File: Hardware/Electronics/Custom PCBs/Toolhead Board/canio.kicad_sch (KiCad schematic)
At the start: 12 parts, among them J7 Conn_01x02, J8 Conn_01x02, J9 120TR, U5 SN65HVD1050D

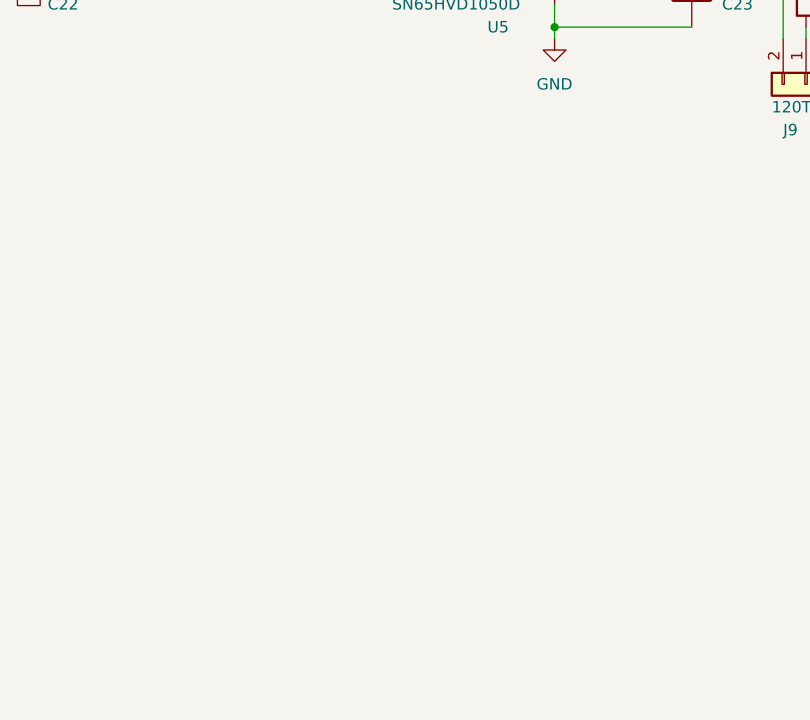
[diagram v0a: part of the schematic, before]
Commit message: Begin replacing CAN transceiver
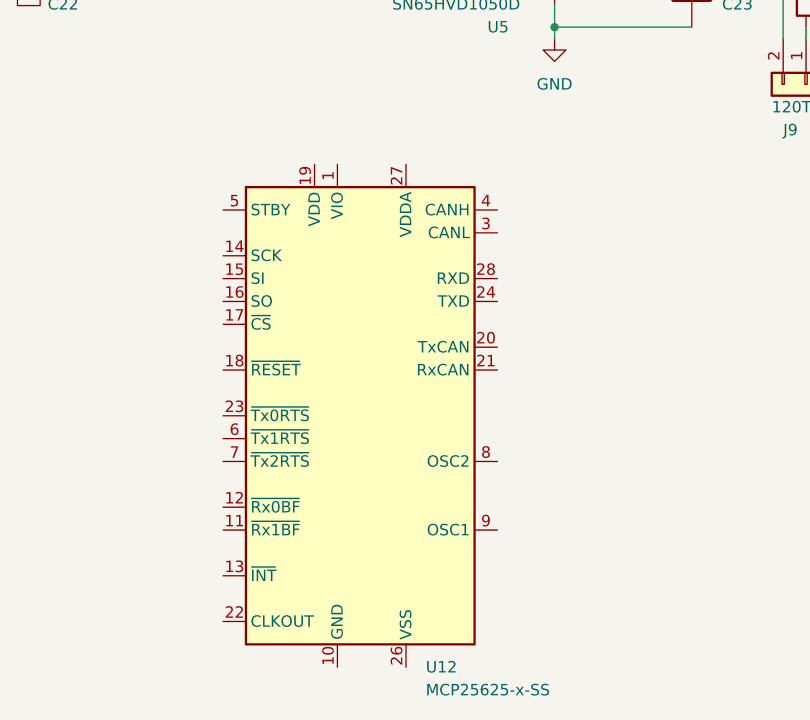
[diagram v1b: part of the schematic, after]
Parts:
- added U12: MCP25625-x-SS, Package_SO:SSOP-28_5.3x10.2mm_P0.65mm, symbol Interface_CAN_LIN:MCP25625-x-SS
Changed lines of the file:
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@@
+	)
+	(symbol
+		(lib_id "Interface_CAN_LIN:MCP25625-x-SS")
+		(at 81.28 96.52 0)
+		(unit 1)
+		(exclude_from_sim no)
+		(in_bom yes)
+		(on_board yes)
+		(dnp no)
+		(fields_autoplaced yes)
+		(property "Reference" "U12"
+			(at 88.5541 124.46 0)
+			(effects
+				(font
+					(size 1.27 1.27)
+				)
+				(justify left)
+			)
+		)
+		(property "Value" "MCP25625-x-SS"
+			(at 88.5541 127 0)
+			(effects
+				(font
+					(size 1.27 1.27)
+				)
+				(justify left)
+			)
+		)
+		(property "Footprint" "Package_SO:SSOP-28_5.3x10.2mm_P0.65mm"
+			(at 83.82 104.14 0)
+			(effects
+				(font
+					(size 1.27 1.27)
+				)
+				(hide yes)
+			)
+		)
+		(property "Datasheet" "http://ww1.microchip.com/downloads/en/DeviceDoc/20005282B.pdf"
+			(at 81.28 81.28 0)
+			(effects
+				(font
+					(size 1.27 1.27)
+				)
+				(hide yes)
+			)
+		)
+		(property "Description" "Stand-Alone CAN Controller with SPI Interface and integated Transceiver, SSOP-28"
+			(at 81.28 96.52 0)
+			(effects
+				(font
+					(size 1.27 1.27)
+				)
+				(hide yes)
+			)
+		)
+		(pin "19"
+		)
+		(pin "18"
+		)
+		(pin "2"
+		)
+		(pin "21"
+		)
+		(pin "14"
+		)
+		(pin "6"
+		)
+		(pin "5"
+		)
+		(pin "15"
+		)
+		(pin "7"
+		)
+		(pin "24"
+		)
+		(pin "4"
+		)
+		(pin "12"
+		)
+		(pin "20"
+		)
+		(pin "28"
+		)
+		(pin "22"
+		)
+		(pin "1"
+		)
+		(pin "16"
+		)
+		(pin "13"
+		)
+		(pin "23"
+		)
+		(pin "25"
+		)
+		(pin "11"
+		)
+		(pin "10"
+		)
+		(pin "26"
+		)
+		(pin "17"
+		)
+		(pin "9"
+		)
+		(pin "3"
+		)
+		(pin "27"
+		)
+		(pin "8"
+		)
+		(instances
+			(project "Toolhead Board"
+				(path "/a1747683-152e-4245-ab61-2d33ce6021ef/ddf7d789-b89f-4838-a0de-61c290d748de"
+					(reference "U12")
+					(unit 1)
+				)
+			)
+		)
 	)
 	(symbol

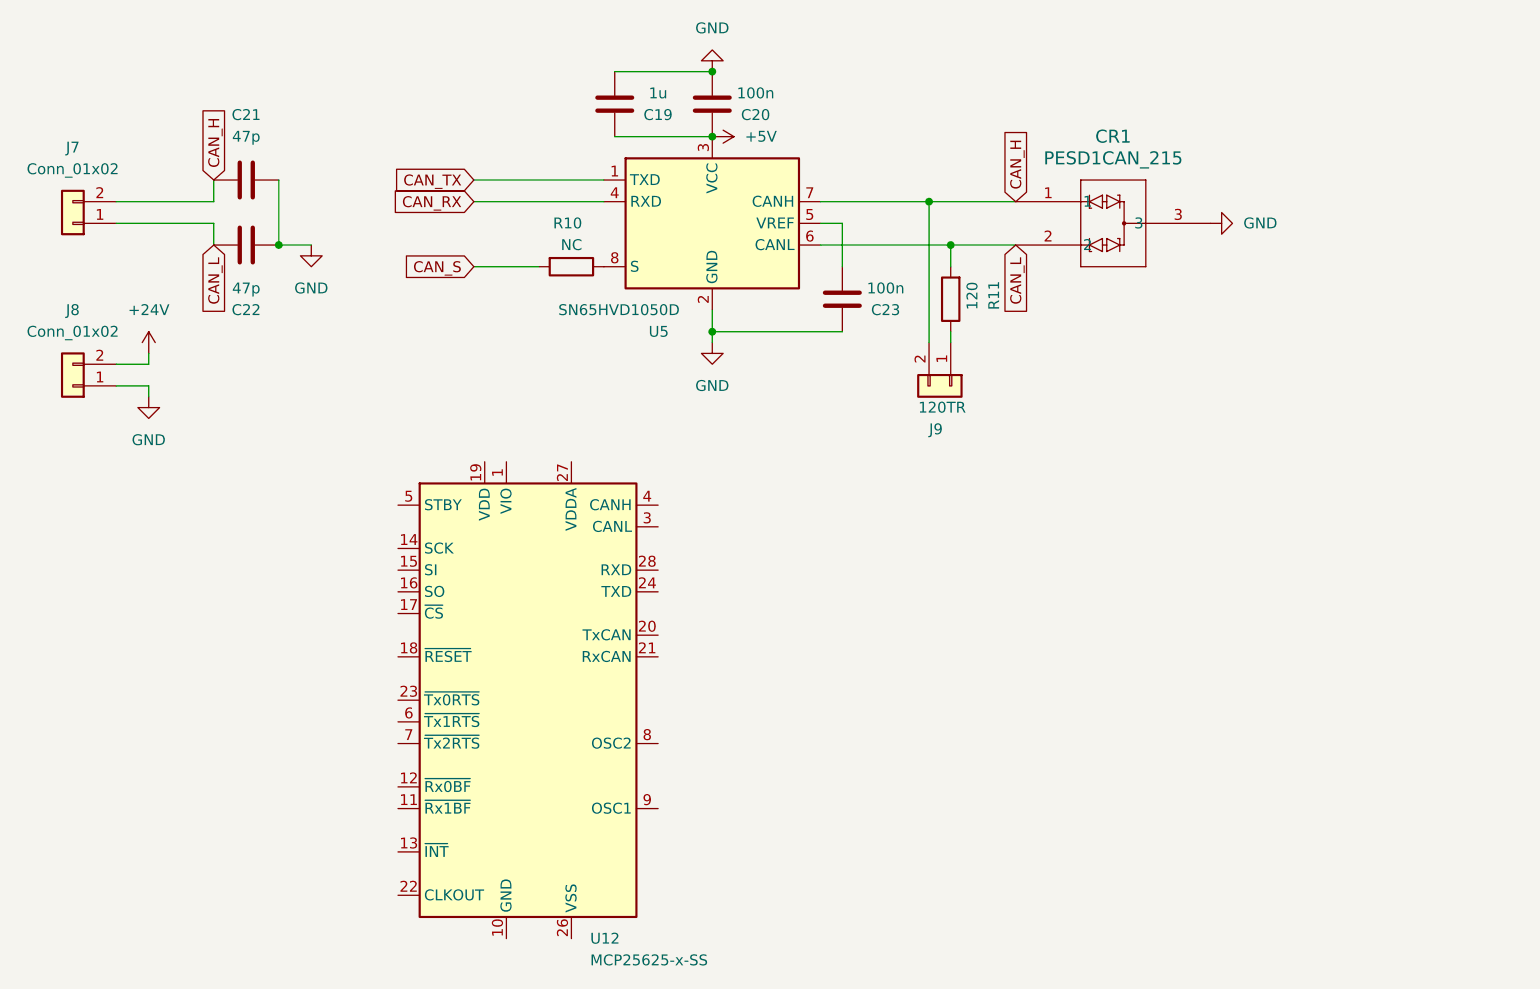
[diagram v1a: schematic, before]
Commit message: Update toolhead schematic+layout and add tolerances to base
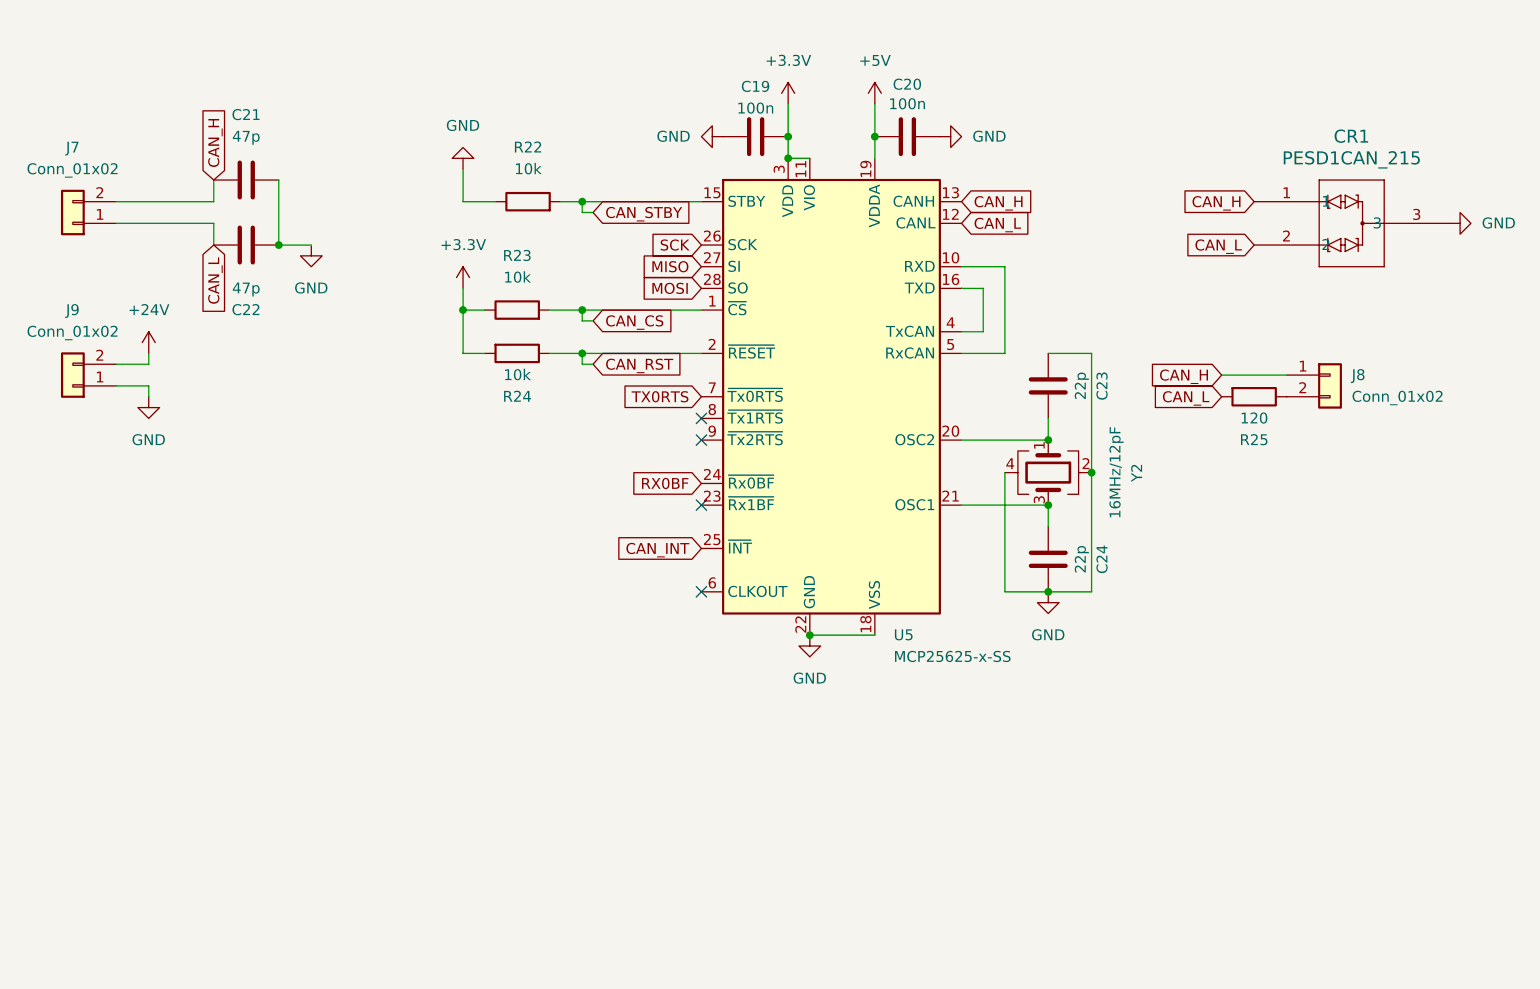
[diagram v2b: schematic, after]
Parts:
- removed J9: 120TR, Connector_PinHeader_2.54mm:PinHeader_1x02_P2.54mm_Vertical, symbol Connector_Generic:Conn_01x02
- removed R10: NC, Resistor_SMD:R_0603_1608Metric_Pad0.98x0.95mm_HandSolder, symbol Device:R
- removed R11: 120, Resistor_SMD:R_0603_1608Metric_Pad0.98x0.95mm_HandSolder, symbol Device:R
- removed U5: SN65HVD1050D, Package_SO:SOIC-8_3.9x4.9mm_P1.27mm, symbol Interface_CAN_LIN:SN65HVD1050D
- added C24: 22p, Capacitor_SMD:C_0603_1608Metric_Pad1.08x0.95mm_HandSolder, symbol Device:C
- added J8: Conn_01x02, Connector_PinHeader_2.54mm:PinHeader_1x02_P2.54mm_Vertical, symbol Connector_Generic:Conn_01x02
- added R22, R23, R24: 10k, Resistor_SMD:R_0603_1608Metric_Pad0.98x0.95mm_HandSolder, symbol Device:R
- added R25: 120, Resistor_SMD:R_0603_1608Metric_Pad0.98x0.95mm_HandSolder, symbol Device:R
- added Y2: 16MHz/12pF, Oscillator:Oscillator_SMD_SeikoEpson_SG210-4Pin_2.5x2.0mm_HandSoldering, symbol Device:Crystal_GND24
- C19: value 1u -> 100n; Digikey 1276-1102-1-ND -> 311-4037-1-ND
- C20: Digikey 1276-1935-1-ND -> 311-4037-1-ND
- C23: value 100n -> 22p; Digikey 1276-1935-1-ND -> 478-KGM15ACG1C220KTCT-ND
- CR1: Digikey 5272-PESD1CANCT-ND -> (none)
- U5: renamed from U12; footprint Package_SO:SSOP-28_5.3x10.2mm_P0.65mm -> Package_DFN_QFN:QFN-28-1EP_6x6mm_P0.65mm_EP4.25x4.25mm
- renumbered J8 to J9
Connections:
- net +5V: now also C20.1, U5.19 (VDDA); no longer C19.2, C20.2
- net CAN_H: now also U5.13 (CANH), J8.1 (Pin_1)
- net CAN_L: now also U5.12 (CANL), R25.2
- net GND: now also C20.2, C23.1, U5.18 (VSS), U5.22 (GND), C24.2, R22.1, Y2.2, Y2.4; no longer C20.1, C23.2
- net CAN_CS: now reaches U5.1 (~{CS})
- net CAN_CS: now also R23.2
- net at U5.10 (RXD): now also U5.5 (RxCAN)
- net +3.3V: now reaches U5.11 (VIO)
- net +3.3V: now also C19.2, U5.3 (VDD), R23.1, R24.2
- net CAN_STBY: now reaches U5.15 (STBY)
- net CAN_STBY: now also R22.2
- net at U5.16 (TXD): now also U5.4 (TxCAN)
- net CAN_RST: now reaches U5.2 (~{RESET})
- net CAN_RST: now also R24.1
- net at U5.20 (OSC2): now also C23.2, Y2.1
- net at U5.21 (OSC1): now also C24.1, Y2.3
- net RX0BF: now reaches U5.24 (~{Rx0BF})
- net CAN_INT: now reaches U5.25 (~{INT})
- net SCK: now reaches U5.26 (SCK)
- net MISO: now reaches U5.27 (SI)
- net MOSI: now reaches U5.28 (SO)
- net TX0RTS: now reaches U5.7 (~{Tx0RTS})
- new net: J8.2 (Pin_2), R25.1
- no-connect marks 0 -> 4
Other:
- moved on the sheet: U5
